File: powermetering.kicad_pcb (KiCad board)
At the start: 2 copper layers, 103 x 103 mm, 115 parts, among them J1 Conn_01x04, J2 Conn_01x02, J3 Conn_01x02, J4 Conn_01x02, J5 Conn_01x02, T1 Transformer_1P_1S, U2 ADE9000, Y1 Crystal

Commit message: add stm32, ethernet phy, hv supply with lnk304
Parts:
- added C35: 3.9µ, Capacitor_SMD:CP_Elec_8x10, F.Cu at (120.0, 96.3)
- added C36: 3.9µ, Capacitor_SMD:CP_Elec_8x10, F.Cu at (120.0, 84.5)
- added C37: 100n, stmbl:C_0603, F.Cu at (283.1, 66.3)
- added C38: 22µ, stmbl:C_0805, F.Cu at (283.3, 70.3)
- added C39: 100n, stmbl:C_0603, F.Cu at (287.6, 66.3)
- added C40: 22µ, stmbl:C_0805, F.Cu at (288.6, 70.3)
- added C41: 100n, stmbl:C_0603, F.Cu at (285.4, 66.3)
- added C42: 22µ, stmbl:C_0805, F.Cu at (285.9, 70.3)
- added C43: 1n, stmbl:C_0603, F.Cu at (305.5, 120.0)
- added C44: 18p, stmbl:C_0603, F.Cu at (300.9, 95.7)
- added C45: 18p, stmbl:C_0603, F.Cu at (287.6, 87.9)
- added C46: 2.2µ, stmbl:C_0603, F.Cu at (295.8, 88.8)
- added C47: 2.2µ, stmbl:C_0603, F.Cu at (304.2, 110.3)
- added C48: 100n, stmbl:C_0603, F.Cu at (301.9, 110.3)
- added C49: 100n, stmbl:C_0603, F.Cu at (292.8, 101.3)
- added C50: 100n, stmbl:C_0603, F.Cu at (291.9, 96.4)
- added C51: 100n, stmbl:C_0603, F.Cu at (289.0, 91.6)
- added C52: 100n, stmbl:C_0603, F.Cu at (283.1, 86.5)
- added C53: 100n, stmbl:C_0603, F.Cu at (302.6, 106.6)
- added C54: 100n, stmbl:C_0603, F.Cu at (298.7, 92.4)
- added C55: 1n, stmbl:C_0603, F.Cu at (291.9, 92.8)
- added C56: 100n, stmbl:C_0603, F.Cu at (304.8, 106.6)
- added C57: 100n, stmbl:C_0603, F.Cu at (285.4, 86.5)
- added C58: 100n, stmbl:C_0603, F.Cu at (302.6, 103.0)
- added C59: 100n, stmbl:C_0603, F.Cu at (123.5, 39.6)
- added C60: 100n, stmbl:C_0603, F.Cu at (115.4, 46.9)
- added C61: 2.2µ, stmbl:C_0603, F.Cu at (129.2, 33.9)
- added C62: 10µ, stmbl:C_0805, F.Cu at (115.8, 44.4)
- added C63: 150n, stmbl:C_1808, F.Cu at (129.4, 95.9)
- added C64: 10µ, stmbl:C_0805, F.Cu at (111.4, 48.8)
- added C65: 100n, stmbl:C_0603, F.Cu at (124.8, 37.0)
- added C66: 10µ, stmbl:C_0805, F.Cu at (119.5, 39.8)
- added C67: 100n, stmbl:C_0603, F.Cu at (129.8, 31.2)
- added C68: 10µ, stmbl:C_0805, F.Cu at (125.2, 34.5)
- added C69: 10µ, stmbl:C_0805, F.Cu at (120.7, 37.1)
- added C70: 10µ, stmbl:C_0805, F.Cu at (111.4, 46.1)
- added C71: 10µ, stmbl:C_0805, F.Cu at (120.7, 34.5)
- added C72: 10µ, stmbl:C_0805, F.Cu at (125.7, 31.4)
- added C73: 150n, stmbl:C_1808, F.Cu at (129.4, 85.0)
- added D18: ABS2, Diode_SMD:Diode_Bridge_Diotec_ABS, F.Cu at (110.6, 110.0)
- added D19: ABS2, Diode_SMD:Diode_Bridge_Diotec_ABS, F.Cu at (119.1, 110.0)
- added D20: ABS10, Diode_SMD:Diode_Bridge_Diotec_ABS, F.Cu at (110.0, 92.0)
- added D21: ABS10, Diode_SMD:Diode_Bridge_Diotec_ABS, F.Cu at (110.0, 85.0)
- added D22: 1.5KExxA, Diode_THT:D_DO-201AE_P15.24mm_Horizontal, F.Cu at (134.8, 97.9)
- added D23: green, stmbl:LED-0805, F.Cu at (305.2, 124.2)
- added D24: green, stmbl:LED-0805, F.Cu at (283.4, 95.8)
- added D25: green, stmbl:LED-0805, F.Cu at (290.2, 100.7)
- added D26: green, stmbl:LED-0805, F.Cu at (302.3, 114.5)
- added D27: green, stmbl:LED-0805, F.Cu at (286.4, 95.5)
- added D28: green, stmbl:LED-0805, F.Cu at (305.2, 114.5)
- added D29: green, stmbl:LED-0805, F.Cu at (302.3, 124.2)
- added D30: green, stmbl:LED-0805, F.Cu at (302.9, 119.4)
- added D31: green, stmbl:LED-0805, F.Cu at (289.4, 95.8)
- added D32: SS34A, stmbl:SMA_Standard, F.Cu at (108.7, 42.8)
- added D33: ES1J R2, stmbl:SMA_Standard, F.Cu at (151.0, 89.7)
- added D34: ES1J R2, stmbl:SMA_Standard, F.Cu at (150.9, 80.5)
- added D35: green, stmbl:LED-0805-SIDE, F.Cu at (121.1, 31.7)
- added H1: MountingHole_Pad, MountingHole:MountingHole_3.2mm_M3_DIN965_Pad, F.Cu at (167.0, 76.0)
- added H2: MountingHole_Pad, MountingHole:MountingHole_3.2mm_M3_DIN965_Pad, F.Cu at (167.0, 92.0)
- added H3: MountingHole_Pad, MountingHole:MountingHole_3.2mm_M3_DIN965_Pad, F.Cu at (167.0, 108.0)
- added H4: MountingHole_Pad, MountingHole:MountingHole_3.2mm_M3_DIN965_Pad, F.Cu at (167.0, 122.0)
- added H5: MountingHole_Pad, MountingHole:MountingHole_3.2mm_M3_DIN965_Pad, F.Cu at (58.0, 76.0)
- added H6: MountingHole_Pad, MountingHole:MountingHole_3.2mm_M3_DIN965_Pad, F.Cu at (58.0, 92.0)
- added H7: MountingHole_Pad, MountingHole:MountingHole_3.2mm_M3_DIN965_Pad, F.Cu at (58.0, 108.0)
- added H8: MountingHole_Pad, MountingHole:MountingHole_3.2mm_M3_DIN965_Pad, F.Cu at (58.0, 122.0)
- added JP1: BOOT0, stmbl:SOLDER_JUMPER, F.Cu at (294.7, 85.2)
- added JP2: Jumper, stmbl:SOLDER_JUMPER, F.Cu at (292.2, 85.2)
- added JP3: Jumper, stmbl:SOLDER_JUMPER, F.Cu at (301.1, 92.1)
- added JP4: Jumper, stmbl:SOLDER_JUMPER, F.Cu at (303.3, 95.8)
- added L5: 10µH 1A, stmbl:SMD_INDUCTOR_32x25, F.Cu at (115.0, 40.8)
- added L6: 1m 250mA, stmbl:NPI31W, F.Cu at (144.4, 85.5)
- added P1: USB_OTG, stmbl:USB_Micro-B, F.Cu at (262.1, 100.2)
- added P2: CONN_01X04, stmbl:Pin_Header_Straight_1x04, F.Cu at (244.2, 103.2)
- added R45: 450k, stmbl:R_1206, F.Cu at (126.3, 96.4)
- added R46: 450k, stmbl:R_1206, F.Cu at (126.3, 84.5)
- added R47: R, stmbl:R_0603, F.Cu at (272.1, 72.4)
- added R48: 6k49, stmbl:R_0603, F.Cu at (272.1, 74.7)
- added R49: 1k, stmbl:R_0603, F.Cu at (275.8, 72.4)
- added R50: 1k, stmbl:R_0603, F.Cu at (272.1, 76.9)
- added R51: 1k, stmbl:R_0603, F.Cu at (275.8, 74.7)
- added R52: 1k, stmbl:R_0603, F.Cu at (279.4, 72.4)
- added R53: 1k, stmbl:R_0603, F.Cu at (275.8, 76.9)
- added R54: 1k, stmbl:R_0603, F.Cu at (279.4, 74.7)
- added R55: 1k, stmbl:R_0603, F.Cu at (279.4, 76.9)
- added R56: 1k, stmbl:R_0603, F.Cu at (294.2, 96.1)
- added R57: 470, stmbl:R_0603, F.Cu at (296.5, 96.1)
- added R58: 1k, stmbl:R_0603, F.Cu at (291.2, 89.1)
- added R59: 1k, stmbl:R_0603, F.Cu at (298.7, 96.1)
- added R60: 470, stmbl:R_0603, F.Cu at (294.2, 92.4)
- added R61: 470, stmbl:R_0603, F.Cu at (304.8, 103.0)
- added R62: 470, stmbl:R_0603, F.Cu at (302.6, 99.3)
- added R63: 470, stmbl:R_0603, F.Cu at (287.6, 84.3)
- added R64: 470, stmbl:R_0603, F.Cu at (296.4, 92.4)
- added R65: 470, stmbl:R_0603, F.Cu at (289.9, 85.5)
- added R66: 470, stmbl:R_0603, F.Cu at (304.8, 99.3)
- added R67: 470, stmbl:R_0603, F.Cu at (293.5, 88.8)
- added R68: 15k, stmbl:R_0603, F.Cu at (119.9, 42.2)
- added R69: 1k, stmbl:R_0603, F.Cu at (119.9, 44.5)
- added R70: 51k, stmbl:R_0603, F.Cu at (115.4, 49.1)
- added R71: 1k, stmbl:R_0603, F.Cu at (128.4, 37.0)
- added R72: 1k, stmbl:R_0603, F.Cu at (119.9, 46.8)
- added R73: 1.5k, stmbl:R_0603, F.Cu at (123.5, 41.9)
- added R74: 15k, stmbl:R_0603, F.Cu at (127.2, 39.2)
- added R75: 3.9k, stmbl:R_0603, F.Cu at (123.5, 44.1)
- added R76: 1k, stmbl:R_0603, F.Cu at (119.1, 49.0)
- added R77: 1k, stmbl:R_0603, F.Cu at (123.5, 46.4)
- added REF**: Symbol_Highvoltage_Type2_CopperTop_Small, Symbol:Symbol_Highvoltage_Type2_CopperTop_Small, F.Cu at (116.8, 72.2)
- added REF**: MountingHole_3.2mm_M3_DIN965, MountingHole:MountingHole_3.2mm_M3_DIN965, F.Cu at (142.4, 134.0)
- added REF**: MountingHole_3.2mm_M3_DIN965, MountingHole:MountingHole_3.2mm_M3_DIN965, F.Cu at (142.4, 58.0)
- added REF**: MountingHole_3.2mm_M3_DIN965, MountingHole:MountingHole_3.2mm_M3_DIN965, F.Cu at (66.4, 134.0)
- added REF**: MountingHole_3.2mm_M3_DIN965, MountingHole:MountingHole_3.2mm_M3_DIN965, F.Cu at (66.4, 58.0)
- added T2: Transformer_1P_1S, Transformer_THT:Transformer_CHK_EI30-2VA_1xSec, F.Cu at (98.0, 142.0)
- added T3: Transformer_1P_1S, Transformer_THT:Transformer_CHK_EI30-2VA_1xSec, F.Cu at (131.0, 142.0)
- added U1: KSZ8081, stmbl:QFN-24-1EP_4x4mm_Pitch0.5mm, F.Cu at (285.1, 75.8)
- added U3: STM32F407VETx, stmbl:LQFP-100_14x14mm_Pitch0.5mm, F.Cu at (243.7, 114.8)
- added U4: USBLC6-4SC6, stmbl:SOT-23-6, F.Cu at (284.0, 90.5)
- added U5: ACT4088, stmbl:SOT-23-6, F.Cu at (107.0, 46.9)
- added U6: LNK304D, stmbl:SOIC-7, F.Cu at (143.7, 96.0)
- added Y2: 25M, stmbl:Crystal_SMD_0603_4Pads, F.Cu at (243.5, 128.1)
- F1, F2, F3, F4: footprint Fuse_Holders_and_Fuses:Fuseholder6x32_Horiz_Open_Schurter0031-8002 -> Fuse:Fuse_2920_7451Metric
- R1, R10, R11, R12, R13, R14, R15, R16, R17, R18, R19, R2, R20, R21, R22, R23, R24, R3, R4, R5, R6, R7, R8, R9: footprint Resistors_SMD:R_0603 -> stmbl:R_0603
- R25, R26, R27, R28, R29, R30, R31, R32, R33, R34, R35, R36, R37, R38, R39, R40, R41, R42, R43, R44: footprint Resistors_SMD:R_2010 -> Resistor_SMD:R_2010_5025Metric
- moved F1 233.7 mm to (70.0, 77.0)
- moved F2 210.0 mm to (79.0, 77.0)
- moved F3 185.7 mm to (89.0, 77.0)
- moved F4 162.8 mm to (98.0, 77.0)
- moved T1 141.1 mm to (98.0, 114.2), turned to 90 degrees
- moved R2 138.4 mm to (229.4, 170.8)
- moved C13 138.4 mm to (228.1, 150.1)
- moved J1 137.3 mm to (84.0, 63.0), turned to 0 degrees
- moved C20 118.4 mm to (194.0, 161.4)
- moved C14 118.4 mm to (182.6, 161.4)
- moved C19 118.4 mm to (216.5, 161.7)
- moved C5 118.4 mm to (237.2, 158.9)
- moved C6 118.4 mm to (205.0, 152.0)
- moved D1 118.4 mm to (208.2, 161.2)
- moved C15 118.4 mm to (201.6, 152.0)
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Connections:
- T1 pad 1: Net-(T1-Pad1) -> L3
- T1 pad 10: (no net) -> Net-(D18-Pad4)
- T1 pad 2: Net-(T1-Pad2) -> (no net)
- T1 pad 3: Net-(T1-Pad3) -> (no net)
- T1 pad 4: Net-(T1-Pad4) -> (no net)
- T1 pad 5: (no net) -> L1
- T1 pad 6: (no net) -> Net-(D19-Pad3)
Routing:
- net L1: track 3.25 -> 42.7 mm
- net L2: track 3.25 -> 34.3 mm
- net VPP: track 0.00 -> 30.9 mm
- net Net-(C35-Pad2): track 0.00 -> 30.6 mm
- net GNDPWR: track 0.00 -> 29.4 mm
- net L3: track 3.25 -> 19.1 mm
- net Net-(F4-Pad2): track 7.41 -> 0.00 mm
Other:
- board size 103 x 103 mm -> 212 x 103 mm
- net class three_phase added: clearance 2.5, trace_width 1, via_dia 0.8, via_drill 0.4
- board text added: "Pls no touchy!"

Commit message: remove xfmrs from top board, no space with 18650 backup battery
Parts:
- removed D18, D19: ABS2, Diode_SMD:Diode_Bridge_Diotec_ABS
- removed D23, D24, D25, D26, D27: green, stmbl:LED-0805
- removed JP2, JP3, JP4: Jumper, stmbl:SOLDER_JUMPER
- removed R56, R59: 1k, stmbl:R_0603
- removed R57, R60, R61, R62, R63: 470, stmbl:R_0603
- removed the REF** at (142.4, 134.0)
- removed the REF** at (142.4, 58.0)
- removed the REF** at (66.4, 134.0)
- removed the REF** at (66.4, 58.0)
- removed the REF** at (251.4, 58.0)
- removed the REF** at (175.4, 58.0)
- removed the REF** at (175.4, 134.0)
- removed the REF** at (251.4, 134.0)
- removed T1, T2, T3: Transformer_1P_1S, Transformer_THT:Transformer_CHK_EI30-2VA_1xSec
- added BT1: Battery_Cell, Battery:BatteryHolder_Keystone_1042_1x18650, F.Cu at (196.0, 149.0)
- added H10: MountingHole, MountingHole:MountingHole_3.2mm_M3, F.Cu at (261.0, 165.0)
- added H11: MountingHole, MountingHole:MountingHole_3.2mm_M3, F.Cu at (151.0, 165.0)
- added H12: MountingHole, MountingHole:MountingHole_3.2mm_M3, F.Cu at (336.0, 165.0)
- added H13: MountingHole, MountingHole:MountingHole_3.2mm_M3, F.Cu at (151.0, 89.0)
- added H14: MountingHole, MountingHole:MountingHole_3.2mm_M3, F.Cu at (261.0, 89.0)
- added H15: MountingHole, MountingHole:MountingHole_3.2mm_M3, F.Cu at (227.0, 89.0)
- added H16: MountingHole, MountingHole:MountingHole_3.2mm_M3, F.Cu at (336.0, 89.0)
- added H9: MountingHole, MountingHole:MountingHole_3.2mm_M3, F.Cu at (227.0, 165.0)
- moved C17 142.6 mm to (310.3, 118.8), turned to 90 degrees
- moved C20 140.5 mm to (327.9, 118.8), turned to 270 degrees
- moved C19 116.9 mm to (325.3, 118.8), turned to 90 degrees
- moved R1 112.4 mm to (308.0, 132.1), turned to 180 degrees
- moved C14 109.0 mm to (282.9, 118.8), turned to 270 degrees
- moved L1 106.6 mm to (253.0, 145.2)
- moved R28 106.6 mm to (267.4, 136.7)
- moved R31 106.6 mm to (262.0, 139.2)
- moved R42 106.6 mm to (259.5, 145.2)
- moved D1 106.2 mm to (311.6, 137.0), turned to 90 degrees
- moved C6 104.4 mm to (308.0, 134.5), turned to 180 degrees
- moved R25 104.4 mm to (266.6, 143.6)
- moved C18 102.7 mm to (312.9, 118.8), turned to 270 degrees
- moved C7 102.0 mm to (308.0, 133.3), turned to 180 degrees
- moved C10 101.2 mm to (295.4, 130.4), turned to 90 degrees
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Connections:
- net ENC_B renamed Net-(U3-Pad42)
- net EN_A renamed Net-(U3-Pad41)
- net EN_B renamed Net-(U3-Pad43)
- net EN_Z renamed Net-(U3-Pad45)
- net Net-(C3-Pad2) renamed /RESET
- net PS_EN renamed Net-(U3-Pad92)
- net ain0 renamed Net-(U3-Pad18)
- net ain1 renamed Net-(U3-Pad23)
- net ain2 renamed Net-(U3-Pad26)
- net ain3 renamed Net-(U3-Pad29)
- net ain4 renamed Net-(U3-Pad30)
- net ain5 renamed Net-(U3-Pad31)
- net ain6 renamed Net-(U3-Pad35)
- net ain7 renamed Net-(U3-Pad36)
- net io0 renamed Net-(U3-Pad69)
- net io1 renamed Net-(U3-Pad84)
- net io10 renamed Net-(U3-Pad63)
- net io11 renamed Net-(U3-Pad79)
- net io12 renamed Net-(U3-Pad62)
- net io13 renamed Net-(U3-Pad78)
- net io2 renamed Net-(U3-Pad68)
- net io3 renamed Net-(U3-Pad83)
- net io4 renamed Net-(U3-Pad88)
- net io5 renamed Net-(U3-Pad82)
- net io6 renamed Net-(U3-Pad65)
- net io7 renamed Net-(U3-Pad81)
- net io8 renamed Net-(U3-Pad64)
- net io9 renamed Net-(U3-Pad80)
- net iso_in0 renamed Net-(U3-Pad53)
- net iso_in1 renamed Net-(U3-Pad54)
- net iso_out0 renamed Net-(U3-Pad57)
- net iso_out1 renamed Net-(U3-Pad58)
- net led0 renamed Net-(U3-Pad9)
- net led1 renamed Net-(U3-Pad8)
- net led2 renamed Net-(U3-Pad7)
- net out0 renamed Net-(U3-Pad2)
- net out1 renamed Net-(U3-Pad3)
- net out2 renamed Net-(U3-Pad4)
- net out3 renamed Net-(U3-Pad5)
- net probe0 renamed Net-(U3-Pad61)
- net probe1 renamed Net-(U3-Pad77)
- net spindle_pwm renamed Net-(U3-Pad59)
- net temp renamed Net-(U3-Pad15)
- C10 pad 2: /UL1N -> /UL3N
- C12 pad 2: /UL3N -> /UL1N
- C21 pad 1: /UL1P -> /UL3P
- C21 pad 2: /UL1N -> /UL3N
- C23 pad 1: /UL3P -> /UL1P
- C23 pad 2: /UL3N -> /UL1N
- C24 pad 2: /UL1P -> /UL3P
- C26 pad 2: /UL3P -> /UL1P
- C49 pad 1: Net-(C49-Pad1) -> GND
- C49 pad 2: Net-(C49-Pad2) -> +3V3
- C50 pad 1: Net-(C50-Pad1) -> GND
- C50 pad 2: Net-(C50-Pad2) -> +3V3
- C51 pad 1: Net-(C51-Pad1) -> GND
- C51 pad 2: Net-(C51-Pad2) -> +3V3
- C52 pad 1: Net-(C52-Pad1) -> GND
- C52 pad 2: Net-(C52-Pad2) -> +3V3
- C53 pad 1: Net-(C53-Pad1) -> GND
- C53 pad 2: Net-(C53-Pad2) -> +3V3
- C54 pad 1: Net-(C54-Pad1) -> GND
- C54 pad 2: Net-(C54-Pad2) -> +3V3
- C56 pad 1: Net-(C56-Pad1) -> GND
- C56 pad 2: Net-(C56-Pad2) -> +3V3
- C57 pad 1: Net-(C57-Pad1) -> GND
- C57 pad 2: Net-(C57-Pad2) -> +3V3
- C58 pad 1: Net-(C49-Pad1) -> GND
- C58 pad 2: Net-(C49-Pad2) -> +3V3
- L1 pad 1: L1 -> L3
- L3 pad 1: L3 -> L1
- R22 pad 1: /UL1P -> /UL3P
- R24 pad 1: /UL3P -> /UL1P
- R25 pad 2: /UL1P -> /UL3P
- R27 pad 2: /UL3P -> /UL1P
- R3 pad 1: /UL1N -> /UL3N
- R5 pad 1: /UL3N -> /UL1N
- U2 pad 19: /UL3N -> /UL1N
- U2 pad 20: /UL3P -> /UL1P
- U2 pad 23: /UL1N -> /UL3N
- U2 pad 24: /UL1P -> /UL3P
- U3 pad 17: DC_LINK -> Net-(U3-Pad17)
- U3 pad 40: ENC_A -> Net-(U3-Pad40)
- U3 pad 44: ENC_Z -> Net-(U3-Pad44)
- U3 pad 55: ENC_Z -> Net-(U3-Pad55)
- U3 pad 56: ENC_A -> Net-(U3-Pad56)
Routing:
- net L3: track 19.1 -> 74.1 mm, vias 0 -> 1
- net /UL1P: track 0.00 -> 45.2 mm
- net /UL3P: track 0.00 -> 44.9 mm
- net /UL2P: track 0.00 -> 36.2 mm
- net L2: track 34.3 -> 68.7 mm, vias 0 -> 1
- net L1: track 42.7 -> 67.1 mm
- net VPP: track 30.9 -> 43.8 mm
- net /UL1N: track 0.00 -> 9.96 mm
- net /UL2N: track 0.00 -> 7.61 mm
- net Net-(D17-Pad2): track 50.0 -> 43.6 mm
- net Net-(D13-Pad2): track 50.2 -> 43.8 mm
- net Net-(D15-Pad2): track 49.9 -> 43.5 mm
- net Net-(D11-Pad2): track 50.2 -> 43.8 mm
- net Net-(D16-Pad1): track 49.8 -> 43.4 mm
- net Net-(D14-Pad1): track 49.8 -> 43.4 mm
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
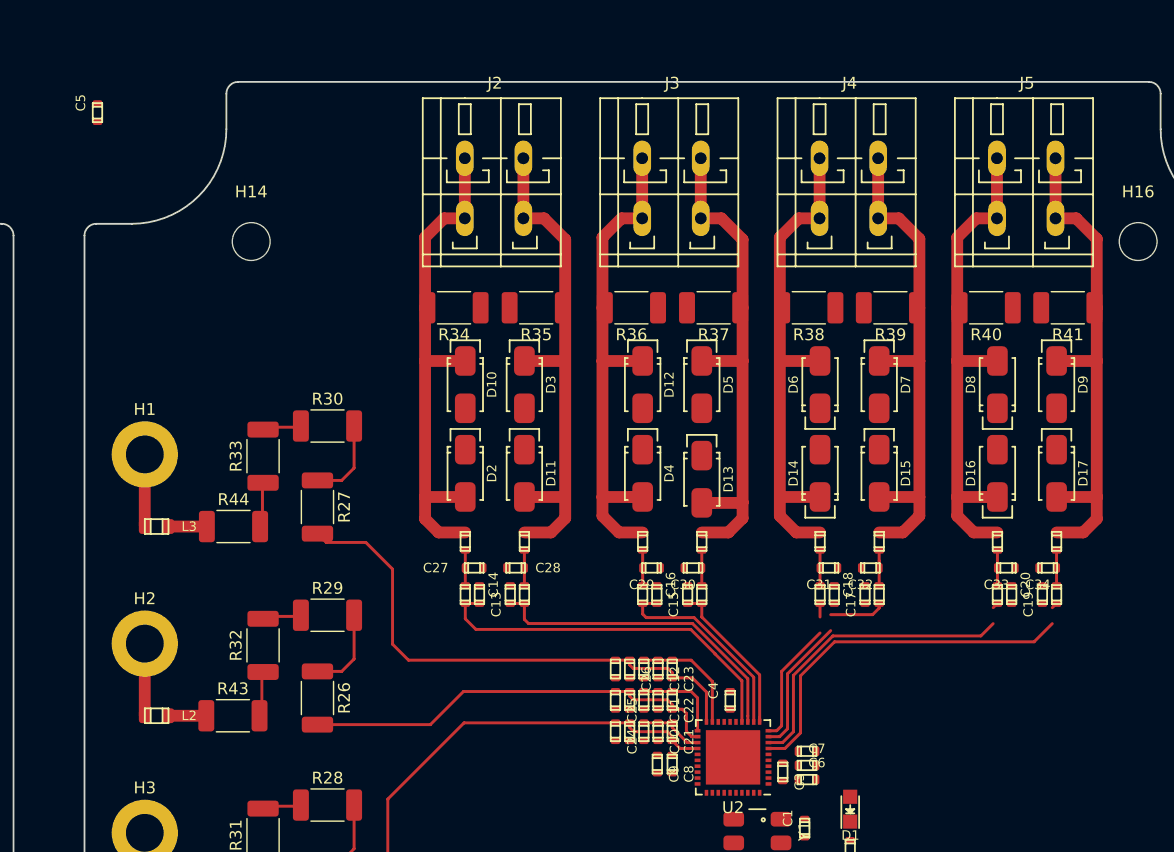
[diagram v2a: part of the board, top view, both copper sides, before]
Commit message: start adding liion charger circuit
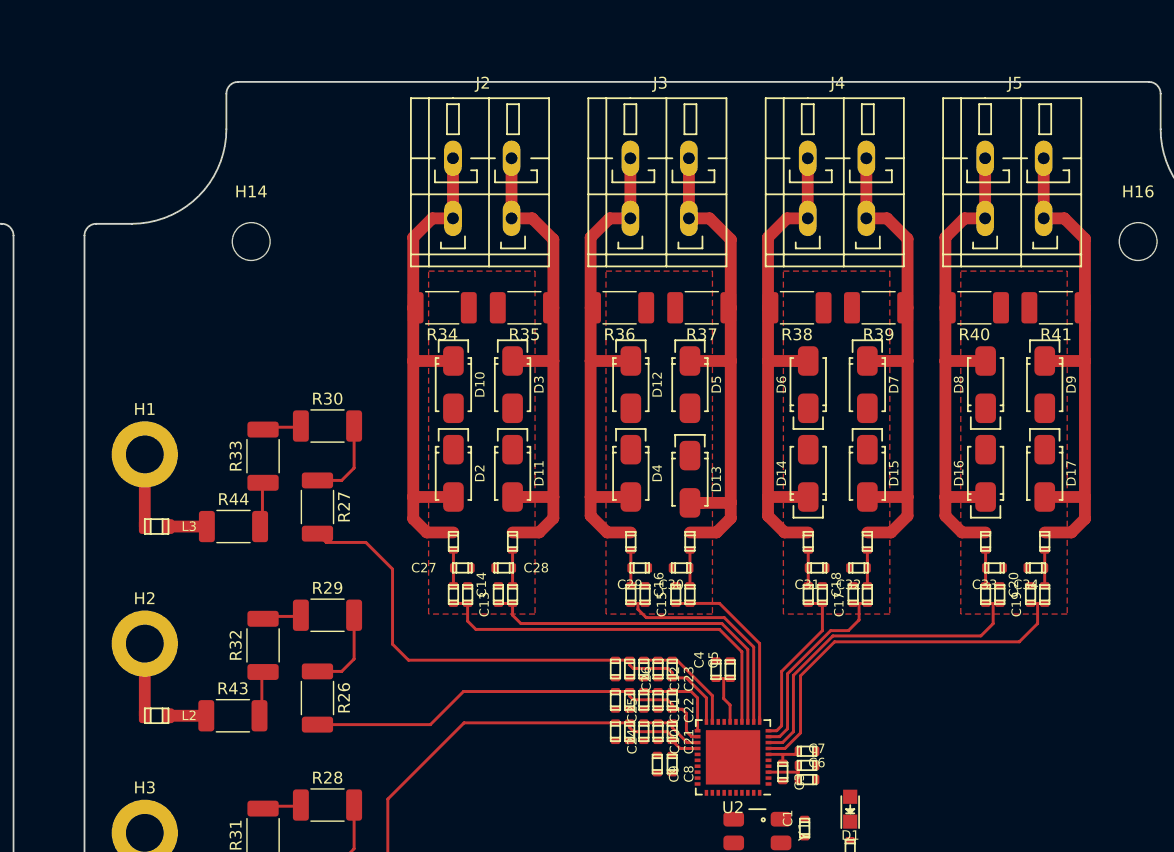
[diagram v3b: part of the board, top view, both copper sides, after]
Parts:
- moved C5 71.3 mm to (301.5, 125.2)
- moved C4 2.86 mm to (300.3, 125.2)
- moved C13 1.00 mm to (279.3, 118.8)
- moved C14 1.00 mm to (281.9, 118.8)
- moved C15 1.00 mm to (294.3, 118.8)
- moved C16 1.00 mm to (296.9, 118.8)
- moved C17 1.00 mm to (309.3, 118.8)
- moved C18 1.00 mm to (311.9, 118.8)
- moved C19 1.00 mm to (324.3, 118.8)
- moved C20 1.00 mm to (326.9, 118.8)
- moved C27 1.00 mm to (278.9, 116.6)
- moved C28 1.00 mm to (282.4, 116.6)
- moved C29 1.00 mm to (293.9, 116.6)
- moved C30 1.00 mm to (297.4, 116.6)
- moved C31 1.00 mm to (308.9, 116.6)
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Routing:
- net /REF: track 0.00 -> 5.09 mm
- net /DVDDOUT: track 0.00 -> 3.71 mm
- net /RESET: track 0.00 -> 3.36 mm
- net /IL3N: track 11.8 -> 14.4 mm
- net /INN: track 26.5 -> 28.9 mm
- net /IL1P: track 27.2 -> 29.4 mm
- net /IL2P: track 13.6 -> 15.5 mm
- net /IL2N: track 17.5 -> 19.1 mm
- net /IL1N: track 31.6 -> 32.9 mm
- net /INP: track 31.7 -> 32.9 mm
- net /UL1N: track 9.96 -> 9.26 mm
- net /IL3P: track 16.4 -> 17.1 mm
- added copper zone on F.Cu, net N

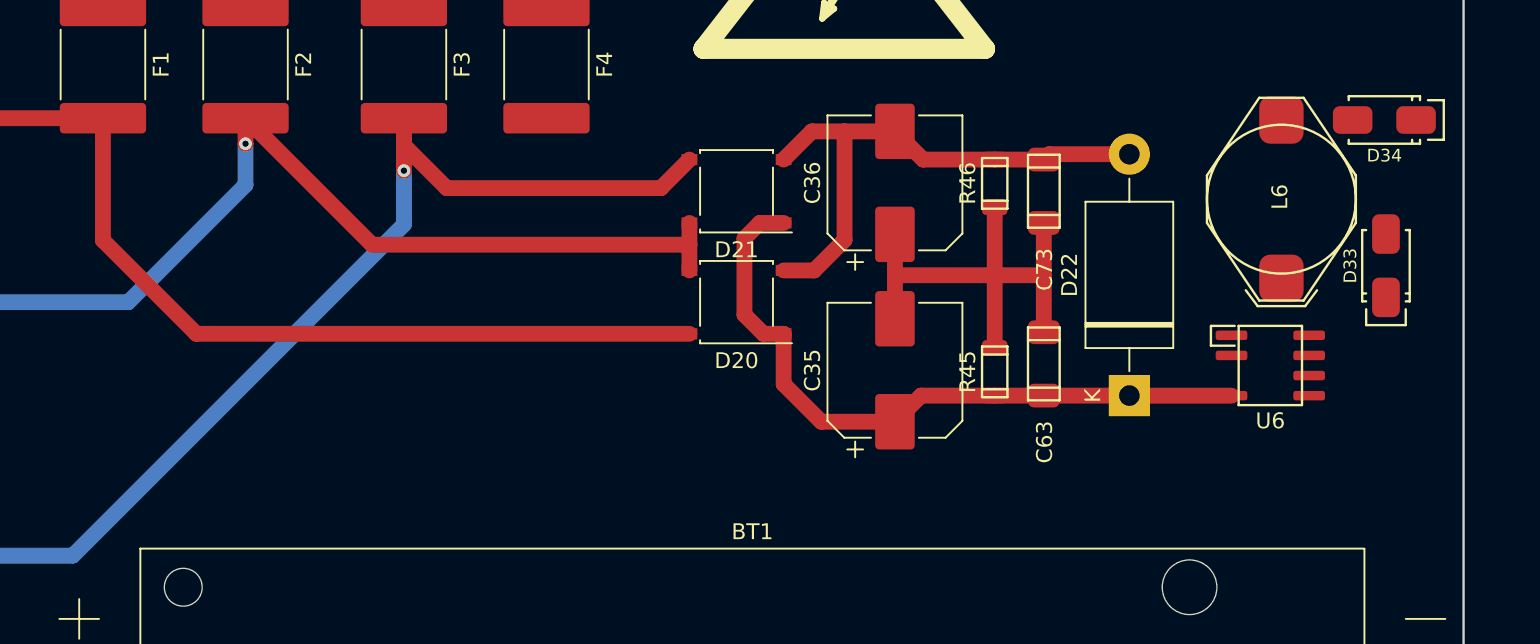
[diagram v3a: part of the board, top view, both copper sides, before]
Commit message: add some 3d models
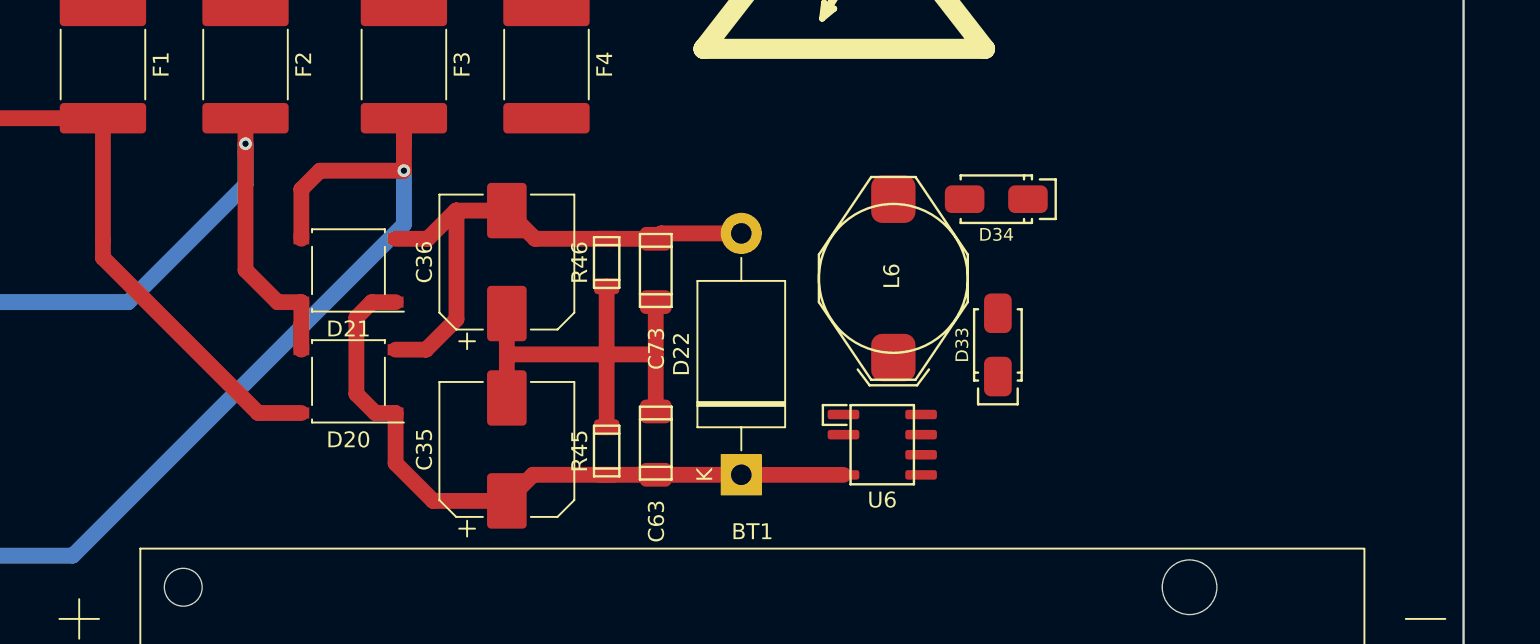
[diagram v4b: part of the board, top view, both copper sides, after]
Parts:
- moved C35 25.0 mm to (180.5, 132.3)
- moved C36 25.0 mm to (180.5, 120.5)
- moved C63 25.0 mm to (189.9, 131.9)
- moved C73 25.0 mm to (189.9, 121.0)
- moved D20 25.0 mm to (170.5, 128.0)
- moved D21 25.0 mm to (170.5, 121.0)
- moved D22 25.0 mm to (195.3, 133.9)
- moved D33 25.0 mm to (211.5, 125.7)
- moved D34 25.0 mm to (211.4, 116.5)
- moved L6 25.0 mm to (204.9, 121.5)
- moved R45 25.0 mm to (186.8, 132.4)
- moved R46 25.0 mm to (186.8, 120.5)
- moved U6 25.0 mm to (204.2, 132.0)
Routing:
- net L1: track 67.1 -> 45.3 mm
- net L2: track 68.7 -> 49.7 mm
- net L3: track 74.1 -> 64.3 mm
